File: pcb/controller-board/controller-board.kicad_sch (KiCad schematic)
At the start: 32 parts, among them J1 SPI_CM5, J10 PWR_IN, J11 Safety, J2 CAN, J6 I2C, J7 HX711, J8 NTC, J9 SWD, U1 STM32G474RETx, U2 AMS1117-3.3, U3 SN65HVD230, Y1 8MHz, Y2 32.77kHz

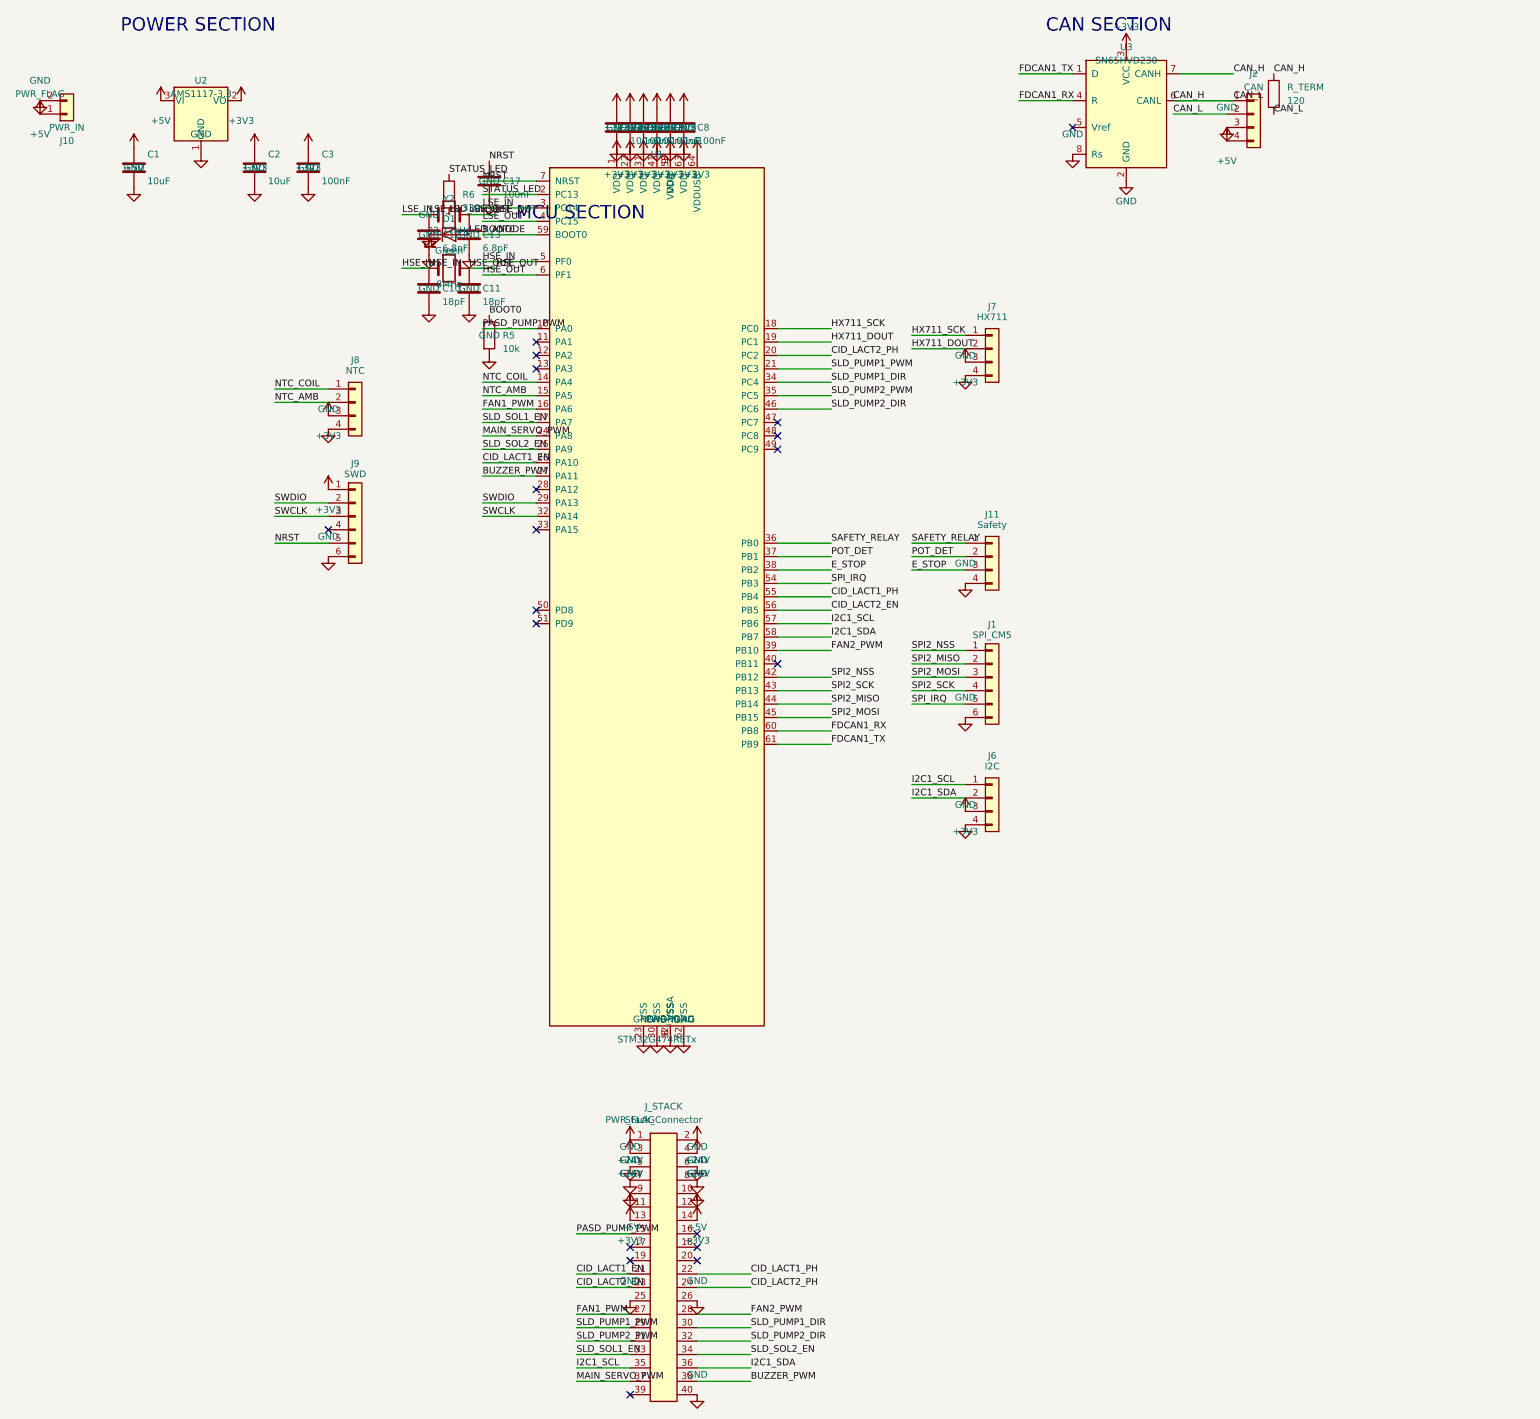
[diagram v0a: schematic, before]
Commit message: Add files via upload
Finalize schematics: 0 ERC errors, subsystem boxes added
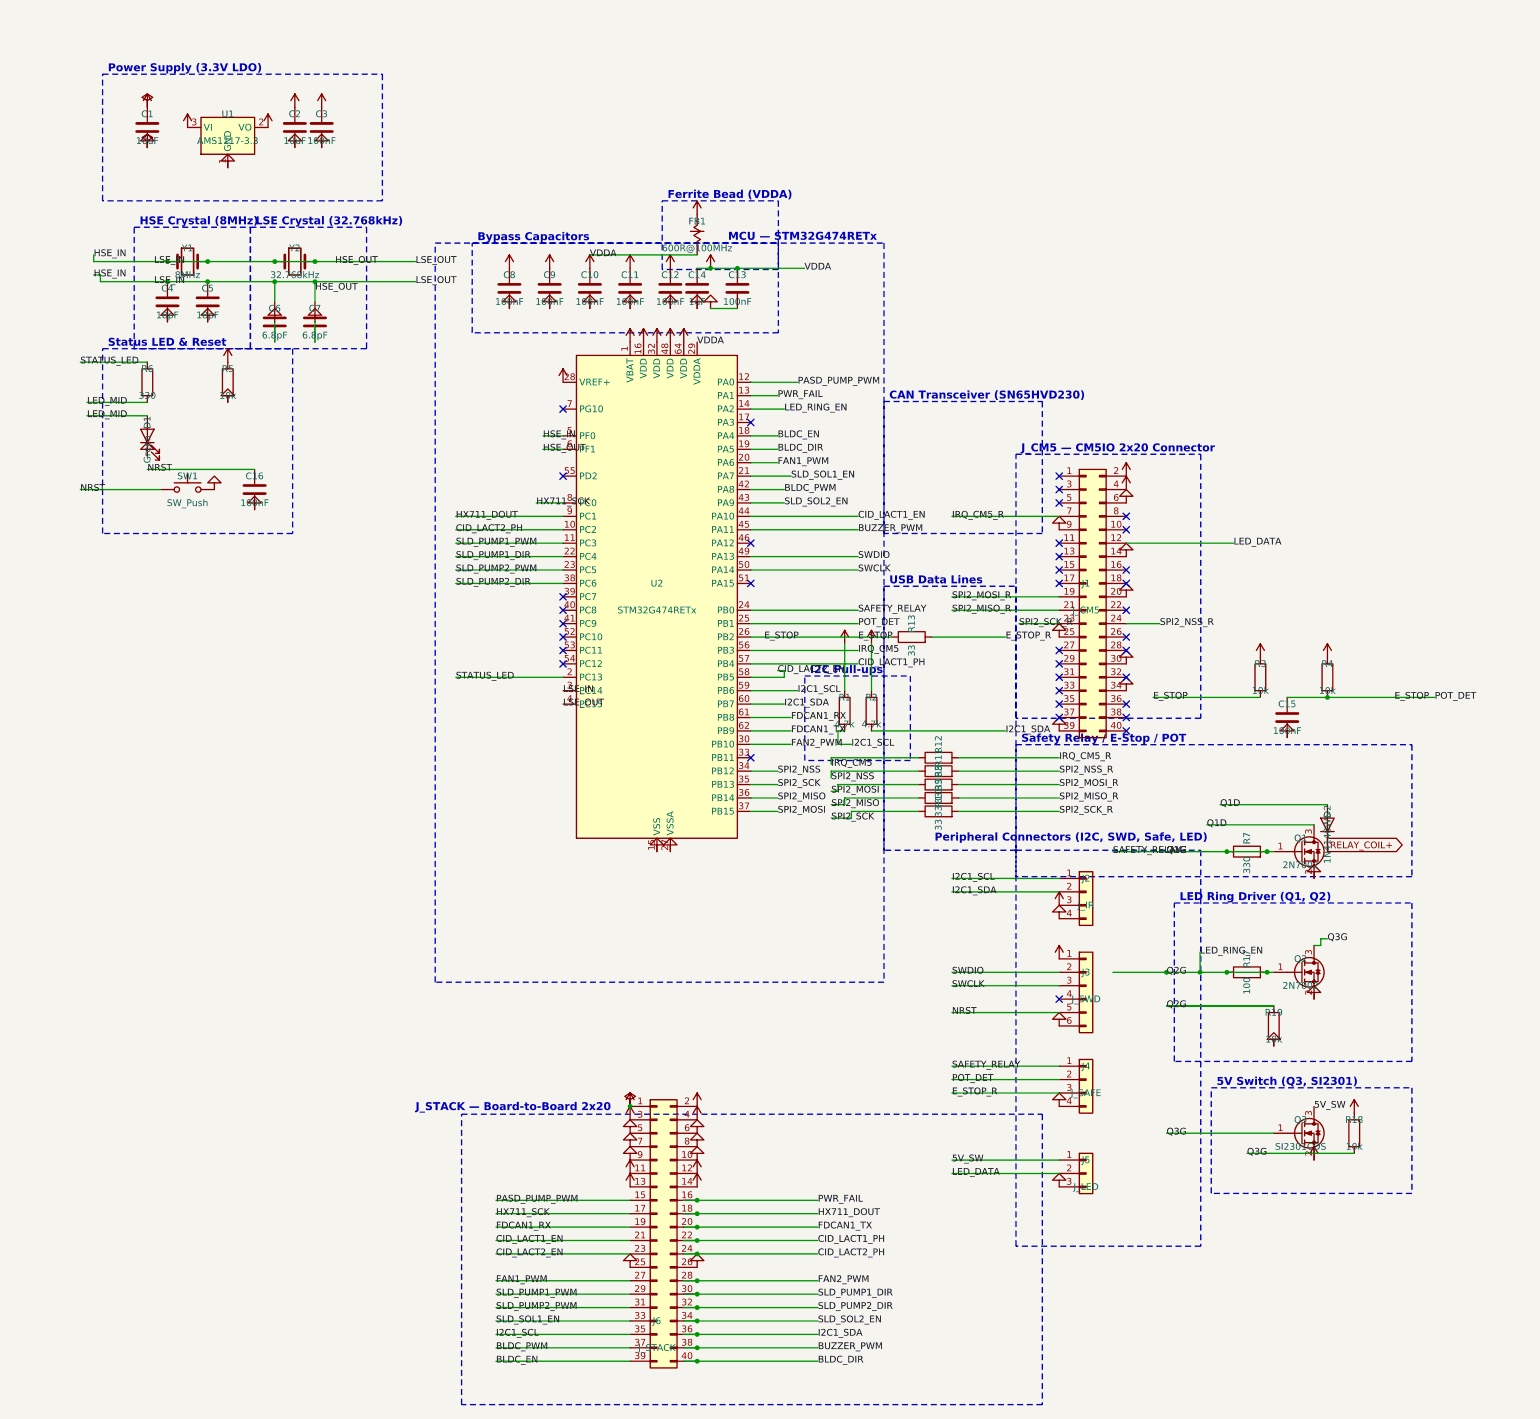
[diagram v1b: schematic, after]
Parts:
- removed C17: 100nF, Capacitor_SMD:C_0402_1005Metric, symbol Device:C
- removed J1: SPI_CM5, Connector_JST:JST_SH_BM06B-SRSS-TB_1x06-1MP_P1.00mm_Vertical, symbol Connector_Generic:Conn_01x06
- removed J10: PWR_IN, Connector_JST:JST_XH_B2B-XH-A_1x02_P2.50mm_Vertical, symbol Connector_Generic:Conn_01x02
- removed J11: Safety, Connector_JST:JST_XH_B4B-XH-A_1x04_P2.50mm_Vertical, symbol Connector_Generic:Conn_01x04
- removed J6: I2C, Connector_JST:JST_SH_BM04B-SRSS-TB_1x04-1MP_P1.00mm_Vertical, symbol Connector_Generic:Conn_01x04
- removed J7: HX711, Connector_JST:JST_XH_B4B-XH-A_1x04_P2.50mm_Vertical, symbol Connector_Generic:Conn_01x04
- removed J8: NTC, Connector_JST:JST_XH_B4B-XH-A_1x04_P2.50mm_Vertical, symbol Connector_Generic:Conn_01x04
- removed J9: SWD, Connector_PinHeader_2.54mm:PinHeader_2x05_P2.54mm_Vertical, symbol Connector_Generic:Conn_01x06
- removed J_STACK: Stack_Connector, Connector_PinHeader_2.54mm:PinHeader_2x20_P2.54mm_Vertical, symbol Connector_Generic:Conn_02x20_Odd_Even
- removed R_TERM: 120, Resistor_SMD:R_0603_1608Metric, symbol Device:R
- removed U1: STM32G474RETx, Package_QFP:LQFP-64_10x10mm_P0.5mm, symbol MCU_ST_STM32G4:STM32G474RETx
- removed U2: AMS1117-3.3, Package_TO_SOT_SMD:SOT-223-3_TabPin2, symbol Regulator_Linear:AMS1117-3.3
- removed U3: SN65HVD230, Package_SO:SOIC-8_3.9x4.9mm_P1.27mm, symbol Interface_CAN_LIN:SN65HVD230
- added C14: 1uF, Capacitor_SMD:C_0402_1005Metric, symbol Device:C
- added C15, C16: 100nF, Capacitor_SMD:C_0402_1005Metric, symbol Device:C
- added D2: 1N4148WS, Diode_SMD:D_SOD-323, symbol Diode:1N4148WS
- added FB1: 600R@100MHz, Inductor_SMD:L_0603_1608Metric, symbol Device:FerriteBead
- added J1: J_CM5, Connector_PinHeader_2.54mm:PinHeader_2x20_P2.54mm_Vertical, symbol Connector_Generic:Conn_02x20_Odd_Even
- added J3: J_SWD, Connector_PinHeader_1.27mm:PinHeader_1x06_P1.27mm_Vertical, symbol Connector_Generic:Conn_01x06
- added J4: J_SAFE, Connector_JST:JST_XH_B4B-XH-A_1x04_P2.50mm_Vertical, symbol Connector_Generic:Conn_01x04
- added J5: J_LED, Connector_JST:JST_XH_B3B-XH-A_1x03_P2.50mm_Vertical, symbol Connector_Generic:Conn_01x03
- added J6: J_STACK, Connector_PinHeader_2.54mm:PinHeader_2x20_P2.54mm_Vertical, symbol Connector_Generic:Conn_02x20_Odd_Even
- added Q1, Q2: 2N7002, Package_TO_SOT_SMD:SOT-23, symbol Transistor_FET:2N7002
- added Q3: SI2301CDS, Package_TO_SOT_SMD:SOT-23, symbol Transistor_FET:2N7002
- added R1, R2: 4.7k, Resistor_SMD:R_0402_1005Metric, symbol Device:R
- added R10, R11, R12, R13, R8, R9: 33, Resistor_SMD:R_0402_1005Metric, symbol Device:R
- added R17: 100, Resistor_SMD:R_0402_1005Metric, symbol Device:R
- added R18, R19, R3, R4: 10k, Resistor_SMD:R_0402_1005Metric, symbol Device:R
- added R7: 330, Resistor_SMD:R_0402_1005Metric, symbol Device:R
- added SW1: SW_Push, Button_Switch_SMD:SW_SPST_TL3342, symbol Switch:SW_Push
- added U1: AMS1117-3.3, Package_TO_SOT_SMD:SOT-223-3_TabPin2, symbol Regulator_Linear:AMS1117-3.3
- added U2: STM32G474RETx, Package_QFP:LQFP-64_10x10mm_P0.5mm, symbol MCU_ST_STM32G4:STM32G474RETx
- C10, C11: value 18pF -> 100nF
- C12, C13: value 6.8pF -> 100nF
- C3: footprint Capacitor_SMD:C_0603_1608Metric -> Capacitor_SMD:C_0402_1005Metric
- C4, C5: value 100nF -> 18pF
- C6, C7: value 100nF -> 6.8pF
- C9: value 1uF -> 100nF
- J2: value CAN -> J_IR; footprint Connector_JST:JST_XH_B4B-XH-A_1x04_P2.50mm_Vertical -> Connector_JST:JST_SH_SM04B-SRSS-TB_1x04-1MP_P1.00mm_Horizontal
- Y2: value 32.77kHz -> 32.768kHz
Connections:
- net BOOT0 is gone; now on net +3V3: R5.1
- net +24V: now also J6.1 (Pin_1), J6.2 (Pin_2), J6.3 (Pin_3), J6.4 (Pin_4)
- net +3V3: now also C10.1, C11.1, C12.1, C13.1, J2.3 (Pin_3), C14.1, FB1.1, FB1.2, J3.1 (Pin_1), J6.13 (Pin_13), J6.14 (Pin_14), R1.1, R2.1, R3.1, R4.1, U1.2 (VO), U2.1 (VBAT), U2.16 (VDD), U2.28 (VREF+), U2.29 (VDDA), U2.32 (VDD), U2.48 (VDD), U2.64 (VDD); no longer C4.1, C5.1, C6.1, C7.1
- net +5V: now also J1.2 (Pin_2), J1.4 (Pin_4), J6.11 (Pin_11), J6.12 (Pin_12), Q3.2 (S), R18.1, U1.3 (VI); no longer J2.4 (Pin_4)
- net BUZZER_PWM: now also J6.38 (Pin_38), U2.45 (PA11)
- net CID_LACT1_EN: now also J6.21 (Pin_21), U2.44 (PA10)
- net CID_LACT1_PH: now also J6.22 (Pin_22), U2.57 (PB4)
- net CID_LACT2_EN: now also J6.23 (Pin_23), U2.58 (PB5)
- net CID_LACT2_PH: now also J6.24 (Pin_24), U2.10 (PC2)
- net E_STOP: now also C15.1, J4.2 (Pin_2), R13.1, R3.2, R4.2, U2.25 (PB1), U2.26 (PB2)
- net FAN1_PWM: now also J6.27 (Pin_27), U2.20 (PA6)
- net FAN2_PWM: now also J6.28 (Pin_28), U2.30 (PB10)
- net FDCAN1_RX: now also J6.19 (Pin_19), U2.61 (PB8)
- net FDCAN1_TX: now also J6.20 (Pin_20), U2.62 (PB9)
- net GND: now also J2.4 (Pin_4), C14.2, C15.2, C16.2, J1.14 (Pin_14), J1.20 (Pin_20), J1.25 (Pin_25), J1.30 (Pin_30), J1.34 (Pin_34), J1.39 (Pin_39), J1.6 (Pin_6), J1.9 (Pin_9), J3.6 (Pin_6), J4.4 (Pin_4), J5.3 (Pin_3), J6.10 (Pin_10), J6.25 (Pin_25), J6.26 (Pin_26), J6.5 (Pin_5), J6.6 (Pin_6), J6.7 (Pin_7), J6.8 (Pin_8), J6.9 (Pin_9), Q1.2 (S), Q2.2 (S), R19.2, SW1.2, U1.1 (GND), U2.15 (VSS), U2.27 (VSSA), U2.31 (VSS), U2.47 (VSS), U2.63 (VSS); no longer J2.3 (Pin_3)
- net HSE_IN: now also C4.1, C5.1, C6.1, C7.1, Y1.2, Y2.1, Y2.2, U2.3 (PC14), U2.4 (PC15), U2.5 (PF0), U2.6 (PF1); no longer C10.1
- net HX711_DOUT: now also J6.18 (Pin_18), U2.9 (PC1)
- net HX711_SCK: now also J6.17 (Pin_17), U2.8 (PC0)
- net I2C1_SCL: now also J2.1 (Pin_1), J6.35 (Pin_35), R1.2, U2.59 (PB6)
- net I2C1_SDA: now also J2.2 (Pin_2), J6.36 (Pin_36), R2.2, U2.60 (PB7)
- net NRST: now also C16.1, J3.5 (Pin_5), SW1.1
- net PASD_PUMP_PWM: now also J6.15 (Pin_15), U2.12 (PA0)
- net SLD_PUMP1_DIR: now also J6.30 (Pin_30), U2.22 (PC4)
- net SLD_PUMP1_PWM: now also J6.29 (Pin_29), U2.11 (PC3)
- net SLD_PUMP2_DIR: now also J6.32 (Pin_32), U2.38 (PC6)
- net SLD_PUMP2_PWM: now also J6.31 (Pin_31), U2.23 (PC5)
- net SLD_SOL1_EN: now also J6.33 (Pin_33), U2.21 (PA7)
- net SLD_SOL2_EN: now also J6.34 (Pin_34), U2.43 (PA9)
- net SPI2_MISO: now also R9.1, U2.36 (PB14)
- net SPI2_MOSI: now also R8.1, U2.37 (PB15)
- net SPI2_NSS: now also R11.1, U2.34 (PB12)
- net SPI2_SCK: now also R10.1, U2.35 (PB13)
- net STATUS_LED: now also U2.2 (PC13)
- net SWCLK: now also J3.3 (Pin_3), U2.50 (PA14)
- net SWDIO: now also J3.2 (Pin_2), U2.49 (PA13)
- removed net CAN_H: J2.1 (Pin_1), J2.2 (Pin_2)
- removed net HSE_OUT: C11.1, Y1.2
- net LED_ANODE renamed LED_MID
- removed net LSE_IN: C12.1, Y2.1
- removed net LSE_OUT: C13.1, Y2.2
- new net 5V_SW: J5.1 (Pin_1), Q3.3 (D)
- new net BLDC_DIR: J6.40 (Pin_40), U2.19 (PA5)
- new net BLDC_EN: J6.39 (Pin_39), U2.18 (PA4)
- new net BLDC_PWM: J6.37 (Pin_37), U2.42 (PA8)
- new net E_STOP_R: J4.3 (Pin_3), R13.2
- new net IRQ_CM5: R12.1, U2.56 (PB3)
- new net IRQ_CM5_R: J1.7 (Pin_7), R12.2
- new net LED_DATA: J1.12 (Pin_12), J5.2 (Pin_2)
- new net LED_RING_EN: Q2.1 (G), R17.1, R17.2, R19.1, U2.14 (PA2)
- new net PWR_FAIL: J6.16 (Pin_16), U2.13 (PA1)
- new net Q1D: D2.2 (A), Q1.3 (D)
- new net Q1G: J4.1 (Pin_1), Q1.1 (G), R7.1, R7.2, U2.24 (PB0)
- new net Q3G: Q2.3 (D), Q3.1 (G), R18.2
- new net RELAY_COIL+: D2.1 (K)
- new net SPI2_MISO_R: J1.21 (Pin_21), R9.2
- new net SPI2_MOSI_R: J1.19 (Pin_19), R8.2
- new net SPI2_NSS_R: J1.24 (Pin_24), R11.2
- new net SPI2_SCK_R: J1.23 (Pin_23), R10.2
- no-connect marks 19 -> 37
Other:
- note added: "5V Switch (Q3, SI2301)"
- note added: "Bypass Capacitors"
- note added: "CAN Transceiver (SN65HVD230)"
- note added: "Ferrite Bead (VDDA)"
- note added: "HSE Crystal (8MHz)"
- note added: "I2C Pull-ups"
- note added: "J_CM5 — CM5IO 2x20 Connector"
- note added: "J_STACK — Board-to-Board 2x20"
- note added: "LED Ring Driver (Q1, Q2)"
- note added: "LSE Crystal (32.768kHz)"
- note added: "MCU — STM32G474RETx"
- note added: "Peripheral Connectors (I2C, SWD, Safe, LED)"
- note added: "Power Supply (3.3V LDO)"
- note added: "Safety Relay / E-Stop / POT"
- note added: "Status LED & Reset"
- note added: "USB Data Lines"
- note removed: "CAN SECTION"
- note removed: "MCU SECTION"
- note removed: "POWER SECTION"
- company: Epicura -> Epicura / Designed by Cyber_Lord

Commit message: Add files via upload
All #146 items resolved. ERC: 0 errors.

Critical fixes:
- D3 + D4 (PRTR5V0U2X) — ESD protection added on SPI and safety lines
- SJ1 solder jumper — PB3 IRQ/SWO select added
- RELAY_COIL+ — connected to +5V rail

Minor fixes:
- U1/U2 ref designators corrected (U1=STM32, U2=AMS1117)
- C14 and PA11 are doc-only updates, will fix in markdown
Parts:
- added D3, D4: PRTR5V0U2X, Package_TO_SOT_SMD:SOT-143B, symbol Diode:PRTR5V0U2X
- added SJ1: IRQ/SWO, Jumper:SolderJumper-3_P1.3mm_Open_Pad1.0x1.5mm, symbol Jumper:SolderJumper_3_Open
- renumbered U2 to U1, U1 to U2
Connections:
- net IRQ_CM5 is gone; now on net +3V3: R12.1, U1.56 (PB3)
- net RELAY_COIL+ is gone; now on net +5V: D2.1 (K)
- net +3V3: now also D3.3 (VCC), D4.3 (VCC), SJ1.1 (A)
- net E_STOP: now also D4.2 (IO1), D4.4 (IO2)
- net GND: now also D3.1 (GND), D4.1 (GND)
- net SPI2_MOSI: now also D3.4 (IO2)
- net SPI2_SCK: now also D3.2 (IO1)
- new net PB3: SJ1.2 (C), SJ1.3 (B)
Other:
- moved on the sheet: R18
